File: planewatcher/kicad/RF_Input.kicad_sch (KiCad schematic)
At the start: 19 parts, among them U2 AP22653AW6-7

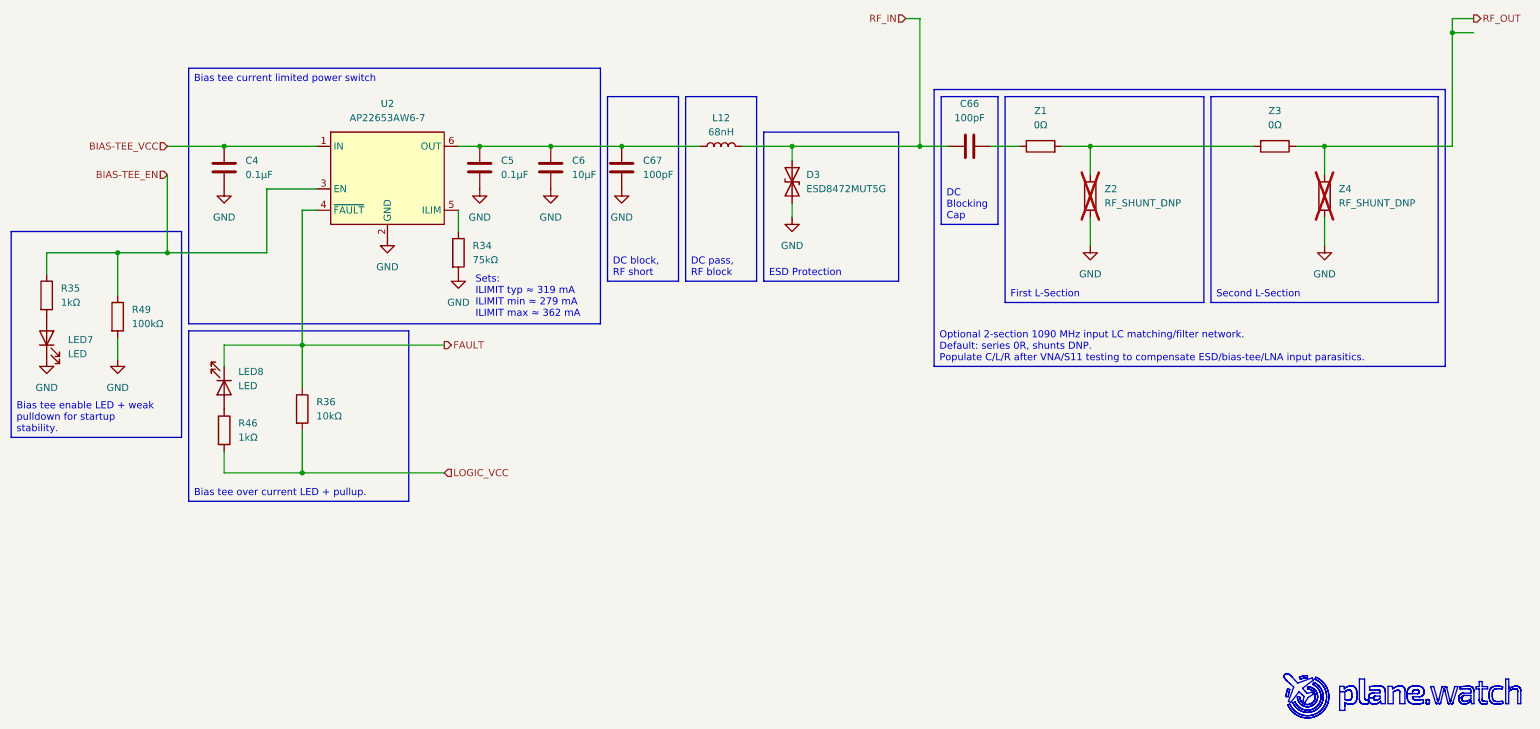
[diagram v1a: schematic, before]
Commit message: Add RF pi matching networks + more
- Remove EEPROM write project solder jumper
- Update proto 1.3 documentation
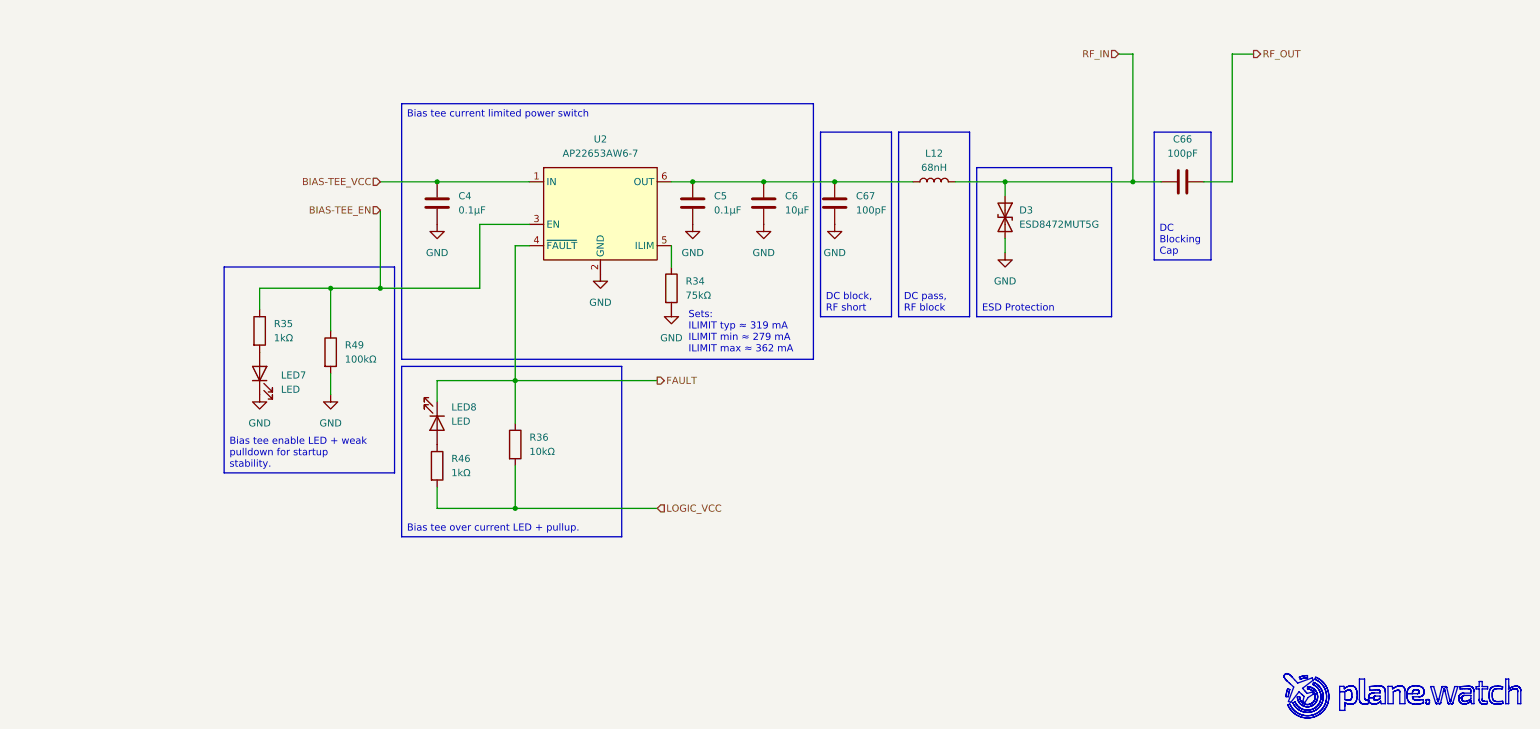
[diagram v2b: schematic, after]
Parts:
- removed Z1, Z3: 0Ω, Resistor_SMD:R_0402_1005Metric, symbol Device:R
- removed Z2, Z4: RF_SHUNT_DNP, Resistor_SMD:R_0402_1005Metric, symbol Device:R
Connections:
- net RF_OUT: now also C66.1
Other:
- moved on the sheet: C4, C5, C6, C66, C67, D3, L12, LED7, LED8, R34, R35, R36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

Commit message: Change LCSC column name, add fabrication toolkit options
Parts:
- C4, C5: LCSC (none) -> C161163; lcsc_id C161163 -> (none)
- C6: LCSC (none) -> C237435; lcsc_id C237435 -> (none)
- C66, C67: LCSC (none) -> C2941926; lcsc_id C2941926 -> (none)
- D3: LCSC (none) -> C133346; lcsc_id C133346 -> (none)
- L12: LCSC (none) -> C3221883; lcsc_id C3221883 -> (none)
- LED7: value LED -> XINGLIGHT XL-1608PGC-06; LCSC (none) -> C7371905; lcsc_id C7371905 -> (none)
- LED8: value LED -> XINGLIGHT XL-1608SURC-06; LCSC (none) -> C965799; lcsc_id C965799 -> (none)
- R34: LCSC (none) -> C482234; lcsc_id C482234 -> (none)
- R35, R46: LCSC (none) -> C106235; lcsc_id C106235 -> (none)
- R36: LCSC (none) -> C191915; lcsc_id C191915 -> (none)
- R49: LCSC (none) -> C481918; lcsc_id C481918 -> (none)
- U2: LCSC (none) -> C1511768; lcsc_id C1511768 -> (none)
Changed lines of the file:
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@@
 			(justify left bottom)
 		)
-		(property "Netclass" "RF_50Ω"
+		(property "Net Class" "RF_50Ω"
 			(at 192.4685 55.88 0)
 			(show_name no)
@@
 			)
 		)
-		(property "lcsc_id" "C161163"
+		(property "LCSC" "C161163"
 			(at 90.17 87.63 0)
 			(hide yes)
@@
 			)
 		)
-		(property "lcsc_id" "C161163"
+		(property "LCSC" "C161163"
 			(at 135.89 87.63 0)
 			(hide yes)
@@
 			)
 		)
-		(property "lcsc_id" "C106235"
+		(property "LCSC" "C106235"
 			(at 90.17 134.62 0)
 			(hide yes)
@@
 			)
 		)
-		(property "lcsc_id" "C482234"
+		(property "LCSC" "C482234"
 			(at 132.08 102.87 0)
 			(hide yes)
@@
 			)
 		)
-		(property "lcsc_id" "C2941926"
+		(property "LCSC" "C2941926"
 			(at 223.52 83.82 0)
 			(hide yes)
@@
 			)
 		)
-		(property "lcsc_id" "C133346"
+		(property "LCSC" "C133346"
 			(at 191.77 90.17 0)
 			(hide yes)
@@
 			)
 		)
-		(property "lcsc_id" "C191915"
+		(property "LCSC" "C191915"
 			(at 104.14 130.81 0)
 			(hide yes)
@@
 			)
 		)
-		(property "Value" "LED"
+		(property "Value" "XINGLIGHT XL-1608SURC-06"
 			(at 92.71 126.6824 90)
 			(show_name no)
@@
 			)
 		)
-		(property "lcsc_id" "C965799"
+		(property "LCSC" "C965799"
 			(at 90.17 127 90)
 			(hide yes)
@@
 			)
 		)
-		(property "lcsc_id" "C1511768"
+		(property "LCSC" "C1511768"
 			(at 119.38 77.47 0)
 			(hide yes)
@@
 			)
 		)
-		(property "lcsc_id" "C2941926"
+		(property "LCSC" "C2941926"
 			(at 161.29 87.63 0)
 			(hide yes)
@@
 			)
 		)
-		(property "lcsc_id" "C481918"
+		(property "LCSC" "C481918"
 			(at 71.12 114.3 0)
 			(hide yes)
@@
 			)
 		)
-		(property "lcsc_id" "C237435"
+		(property "LCSC" "C237435"
 			(at 148.59 87.63 0)
 			(hide yes)
@@
 			)
 		)
-		(property "lcsc_id" "C3221883"
+		(property "LCSC" "C3221883"
 			(at 179.07 83.82 0)
 			(hide yes)
@@
 			)
 		)
-		(property "lcsc_id" "C106235"
+		(property "LCSC" "C106235"
 			(at 58.42 110.49 0)
 			(hide yes)
@@
 			)
 		)
-		(property "Value" "LED"
+		(property "Value" "XINGLIGHT XL-1608PGC-06"
 			(at 62.23 120.9674 90)
 			(show_name no)
@@
 			)
 		)
-		(property "lcsc_id" "C7371905"
+		(property "LCSC" "C7371905"
 			(at 58.42 118.11 90)
 			(hide yes)

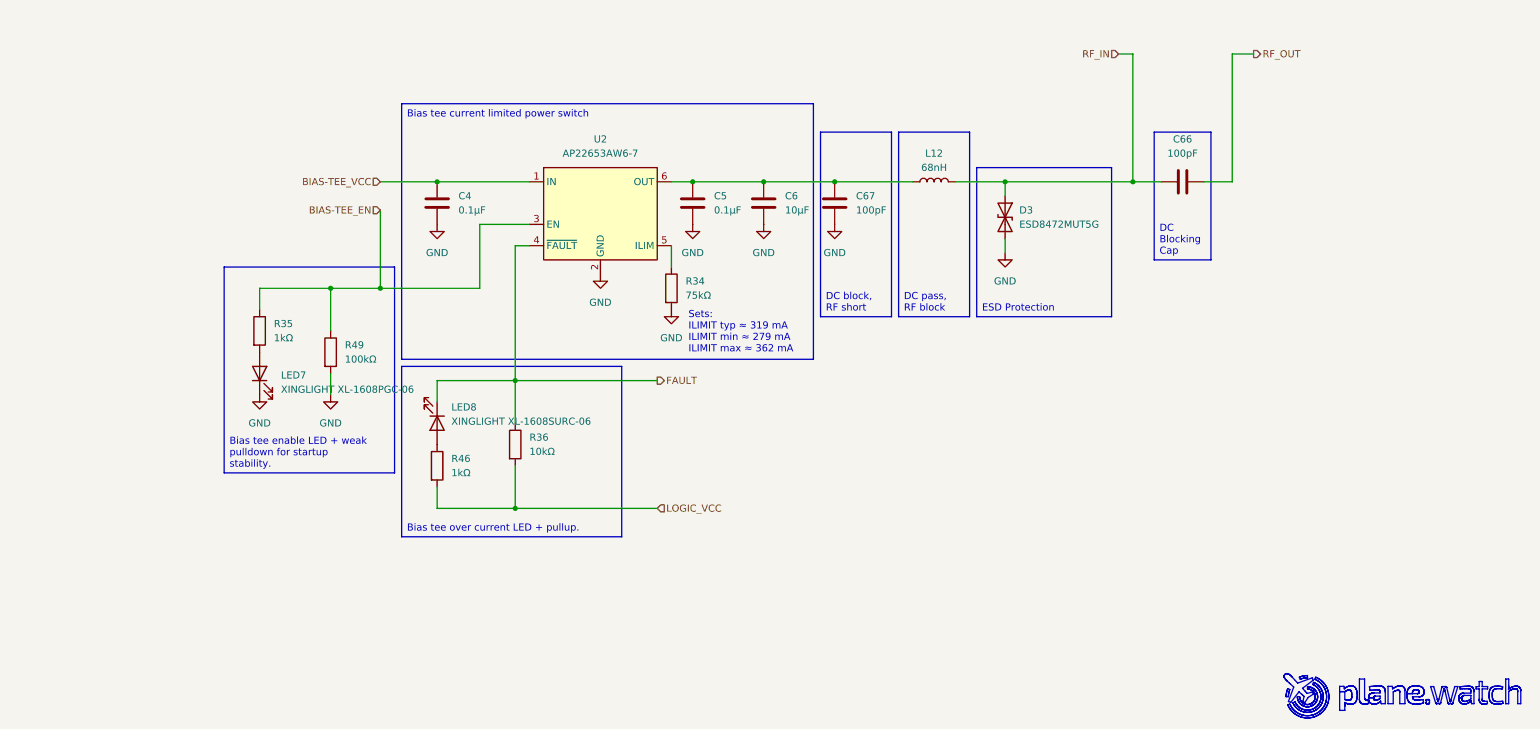
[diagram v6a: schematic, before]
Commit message: Add comments & markup to schematic
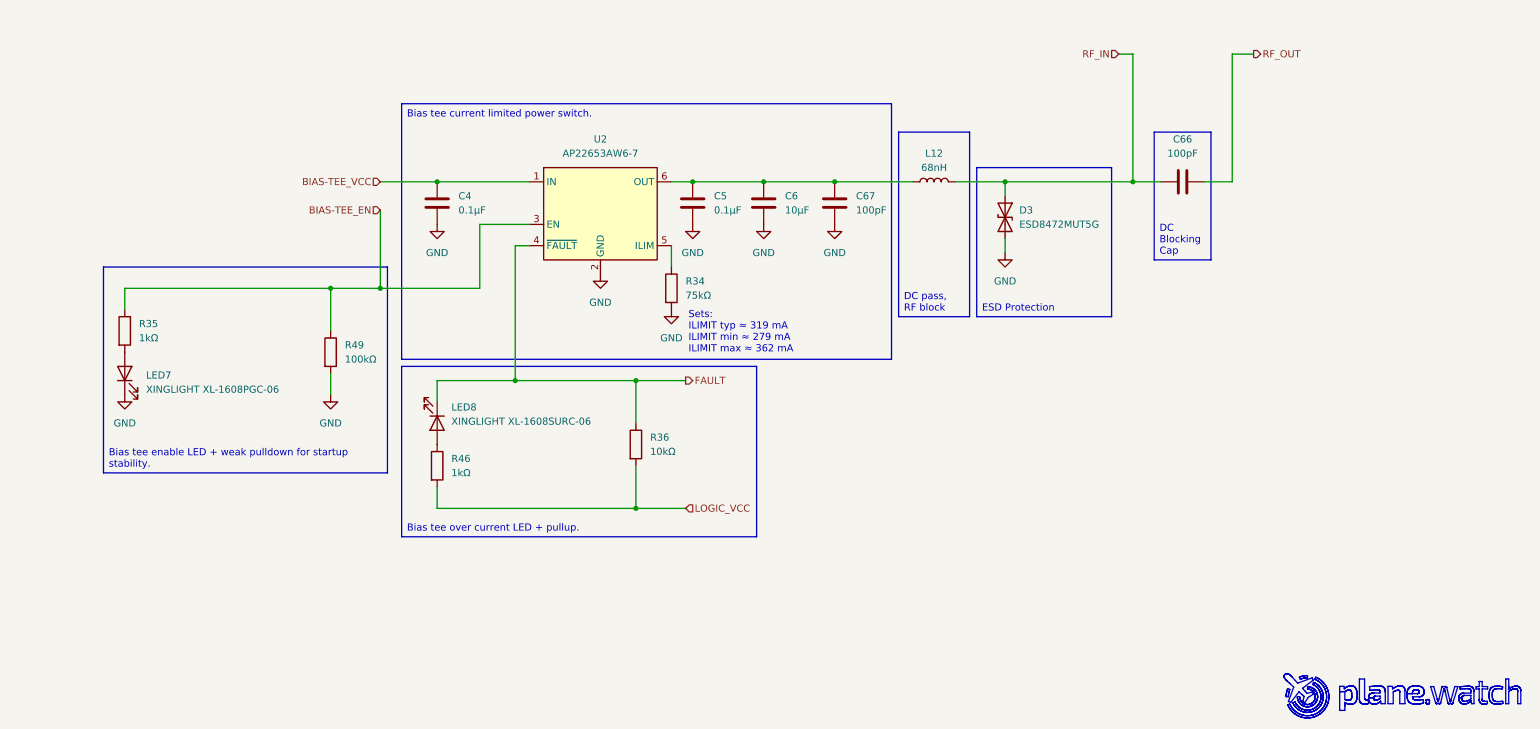
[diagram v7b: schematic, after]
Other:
- moved on the sheet: LED7, R35, R36
